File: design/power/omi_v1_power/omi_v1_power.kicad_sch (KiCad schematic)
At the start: 1 part

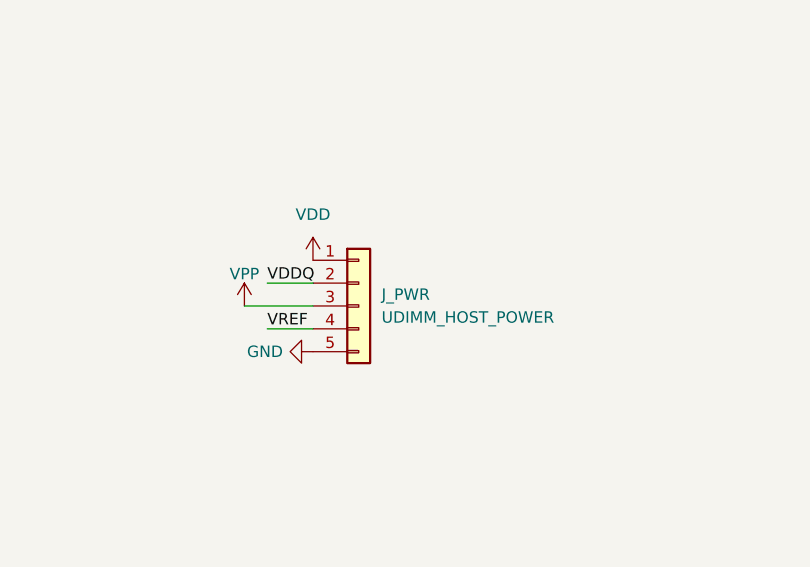
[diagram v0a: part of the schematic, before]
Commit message: feat(phase3): remove redundant root host-power placeholder block (J_PWR + power syms)
J_PWR (UDIMM_HOST_POWER) and its power-distribution symbols #PWR04/05/06
(VPP/VDD/GND) + wires + VREF/VDDQ stub labels were a host-power placeholder
cartoon, now fully superseded by J1 which carries VDD/VPP/GND on real pins
(verified VDD=91, VPP=21, GND=200, VREF=9 nodes, all {J1, DRAMs(+SPD)}).

Removing J_PWR alone orphaned #PWR04/05/06 (3 new pin_not_connected + 1
unconnected_wire_endpoint), so the whole block is removed as one unit. Clears
both root label_dangling (VREF/VDDQ stubs) + the same_local_global (last local
VREF gone) + the "schematic has annotation errors" warning (last non-numeric
ref gone). Root sheet is now a clean hierarchical container (4 sheet boxes).

power_pin_not_driven total unchanged at 5: the GND not-driven relocated from the
placeholder #PWR06 to the actual DRAM GND pin (root -1, acc +1) -> a P5 item.
ERC 88 -> 85. Netlist parses; no net connectivity split.

Co-Authored-By: Claude Opus 4.8 (1M context) <noreply@anthropic.com>
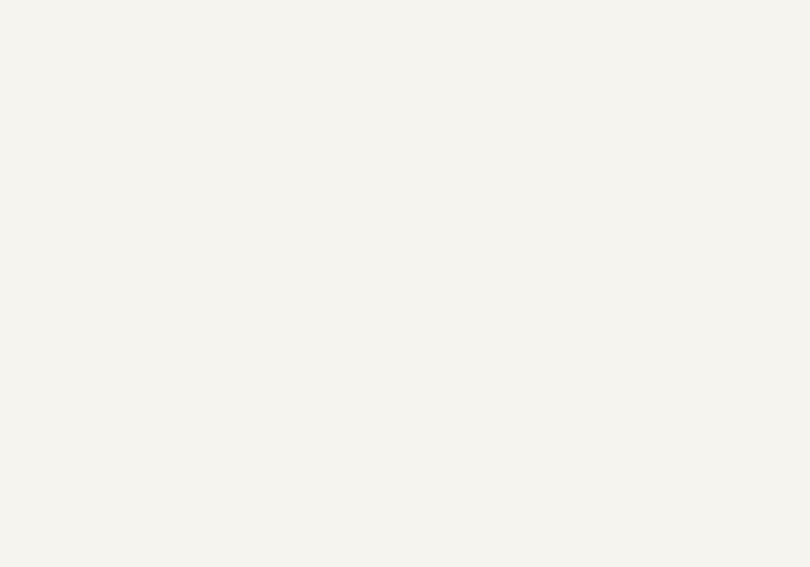
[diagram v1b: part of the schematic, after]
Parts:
- removed J_PWR: UDIMM_HOST_POWER, symbol Connector_Generic:Conn_01x05

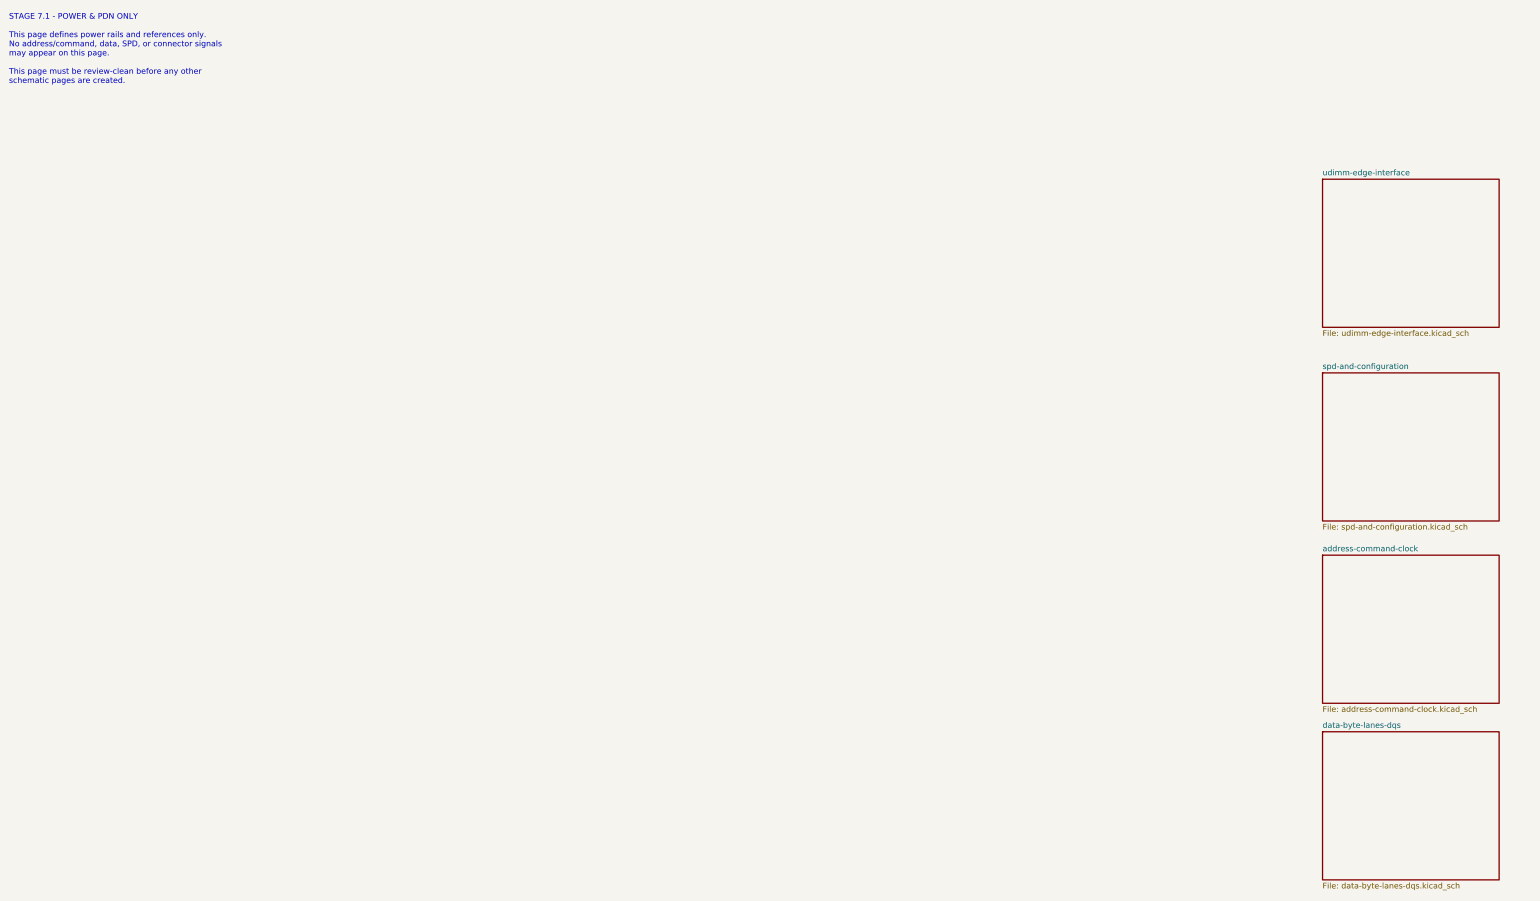
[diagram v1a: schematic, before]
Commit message: polish(schematic): v1.1.0 title blocks + sheet annotations (no electrical change)
Hand-done KiCad 9 GUI pass over all five schematic sheets. Title-block
and text-box content only — no wiring, no component, no net changes.

- Title block (all sheets): Company=OMI, Rev=1.1.0, Date=2026-06-02,
  plus functional per-sheet titles.
- Repurposed the previously-empty DQ/DQS sheet into a byte-lane reference table.
- Added a mechanical caveat text box on the edge (UDIMM) sheet.
- Added a power-rail summary text box on the root sheet.
- omi_v1_power.kicad_prl: project-local UI state saved with the GUI session.

Electrical integrity is asserted to be unchanged and is verified downstream
by the export pipeline (ERC=0 gate + byte-identical netlist and BOM).

Co-Authored-By: Claude Opus 4.8 (1M context) <noreply@anthropic.com>
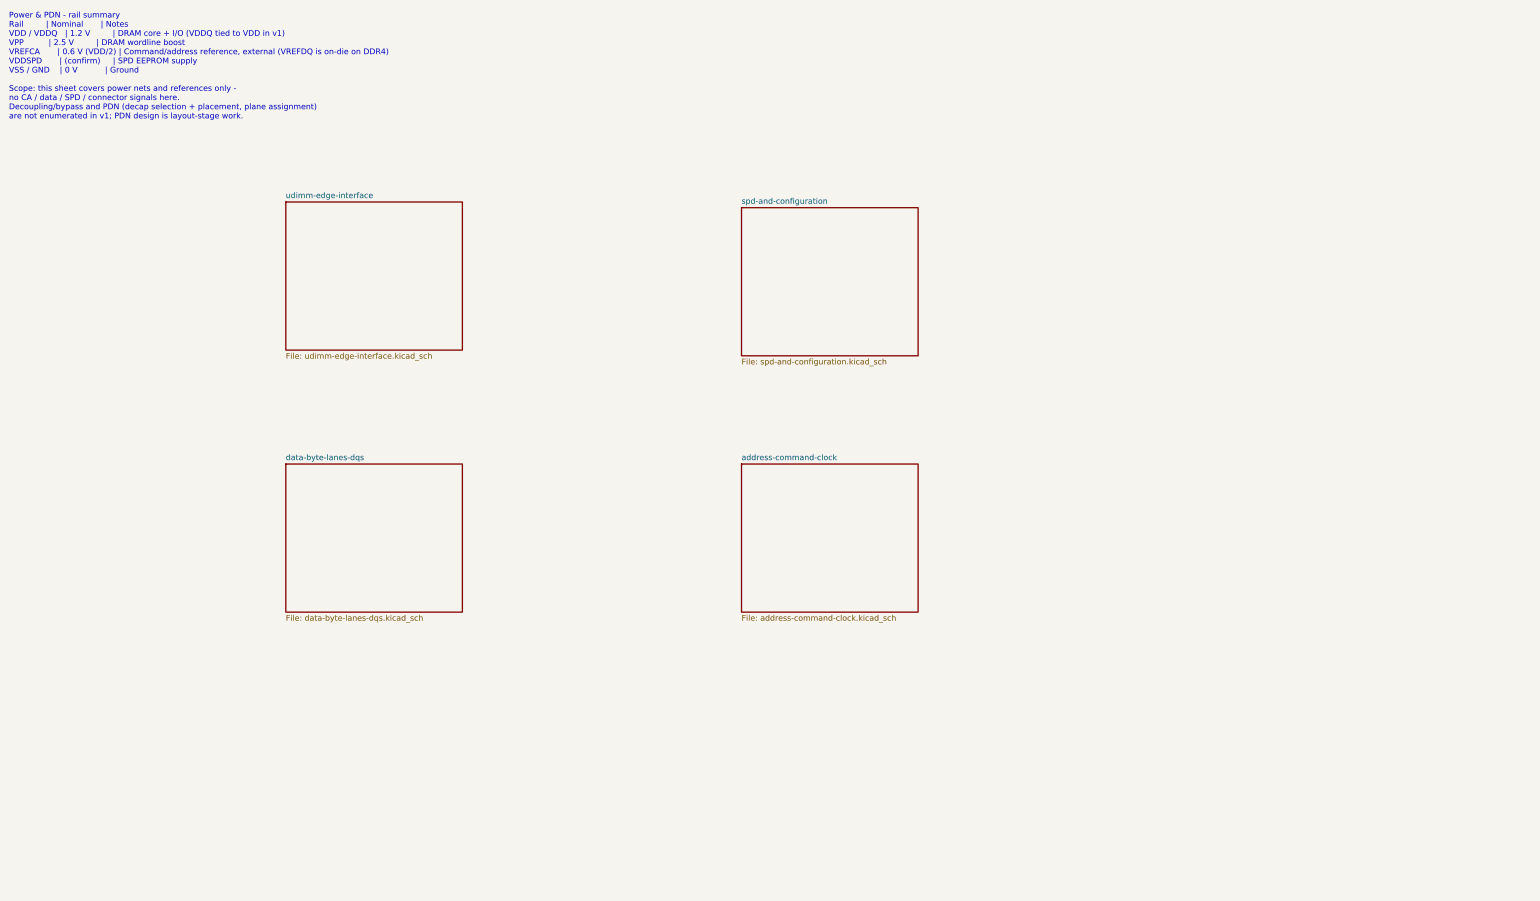
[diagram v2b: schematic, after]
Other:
- note added: "Power & PDN - rail summary Rail | Nominal | Notes VDD / VDDQ | 1.2 V | DRAM core + I/O (VDDQ tied to VDD in v1) VPP | 2.5 V | DRAM wordline boost VREFCA | 0.6 V (VDD/2) | Command/address reference, external (VREFDQ is on-die on DDR4) VDDSPD | (confirm) | SPD EEPROM supply VSS / GND | 0 V | Ground Scope: this sheet covers power nets and references only - no CA / data / SPD / connector signals here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"
- note removed: "STAGE 7.1 - POWER & PDN ONLY This page defines power rails and references only. No address/command, data, SPD, or connector signals may appear on this page. This page must be review-clean before any other schematic pages are created."
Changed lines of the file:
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@@
 	(title_block
 		(title "Power & PDN")
-		(date "2026-01-27")
+		(date "2026-06-02")
 		(rev "1.1.0")
 		(company "OMI")
@@
 		(comment 2 "No CA, Data, SPD, or Connector signals allowed")
 	)
-	(text "STAGE 7.1 - POWER & PDN ONLY\n\nThis page defines power rails and references only.\nNo address/command, data, SPD, or connector signals\nmay appear on this page.\n\nThis page must be review-clean before any other\nschematic pages are created.\n"
+	(text "Power & PDN - rail summary\nRail         | Nominal       | Notes\nVDD / VDDQ   | 1.2 V         | DRAM core + I/O (VDDQ tied to VDD in v1)\nVPP          | 2.5 V         | DRAM wordline boost\nVREFCA       | 0.6 V (VDD/2) | Command/address reference, external (VREFDQ is on-die on DDR4)\nVDDSPD       | (confirm)     | SPD EEPROM supply\nVSS / GND    | 0 V           | Ground\n\nScope: this sheet covers power nets and references only -\nno CA / data / SPD / connector signals here.\nDecoupling/bypass and PDN (decap selection + placement, plane assignment)\nare not enumerated in v1; PDN design is layout-stage work."
 		(exclude_from_sim no)
-		(at 15.748 23.114 0)
+		(at 15.748 26.924 0)
 		(effects
 			(font
@@
 	)
 	(sheet
-		(at 308.61 135.89)
+		(at 179.07 115.57)
 		(size 39.37 33.02)
 		(exclude_from_sim no)
@@
 		)
 		(property "Sheetname" "address-command-clock"
-			(at 308.61 135.1784 0)
+			(at 179.07 114.8584 0)
 			(effects
 				(font
@@
 		)
 		(property "Sheetfile" "address-command-clock.kicad_sch"
-			(at 308.61 169.4946 0)
+			(at 179.07 149.1746 0)
 			(effects
 				(font
@@
 	)
 	(sheet
-		(at 308.61 95.25)
+		(at 179.07 58.42)
 		(size 39.37 33.02)
 		(exclude_from_sim no)
@@
 		)
 		(property "Sheetname" "spd-and-configuration"
-			(at 308.61 94.5384 0)
+			(at 179.07 57.7084 0)
 			(effects
 				(font
@@
 		)
 		(property "Sheetfile" "spd-and-configuration.kicad_sch"
-			(at 308.61 128.8546 0)
+			(at 179.07 92.0246 0)
 			(effects
 				(font
@@
 	)
 	(sheet
-		(at 308.61 52.07)
+		(at 77.47 57.15)
 		(size 39.37 33.02)
 		(exclude_from_sim no)
@@
 		)
 		(property "Sheetname" "udimm-edge-interface"
-			(at 308.61 51.3584 0)
+			(at 77.47 56.4384 0)
 			(effects
 				(font
@@
 		)
 		(property "Sheetfile" "udimm-edge-interface.kicad_sch"
-			(at 308.61 85.6746 0)
+			(at 77.47 90.7546 0)
 			(effects
 				(font
@@
 	)
 	(sheet
-		(at 308.61 175.26)
+		(at 77.47 115.57)
 		(size 39.37 33.02)
 		(exclude_from_sim no)
@@
 		)
 		(property "Sheetname" "data-byte-lanes-dqs"
-			(at 308.61 174.5484 0)
+			(at 77.47 114.8584 0)
 			(effects
 				(font
@@
 		)
 		(property "Sheetfile" "data-byte-lanes-dqs.kicad_sch"
-			(at 308.61 208.8646 0)
+			(at 77.47 149.1746 0)
 			(effects
 				(font
